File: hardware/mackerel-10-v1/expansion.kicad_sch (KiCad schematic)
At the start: 0 parts

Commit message: Rough layout of components on PCB
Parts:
- added C11, C12: 1000uF, Capacitor_THT:CP_Radial_D8.0mm_P3.50mm, symbol Device:C_Polarized
- added J10, J11: Conn_02x20_Odd_Even, Connector_IDC:IDC-Header_2x20_P2.54mm_Vertical, symbol Connector_Generic:Conn_02x20_Odd_Even
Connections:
- new net +5V: C11.1, C12.1, J10.1 (Pin_1), J10.2 (Pin_2), J11.1 (Pin_1), J11.2 (Pin_2)
- new net A1: J10.13 (Pin_13)
- new net A10: J10.28 (Pin_28)
- new net A11: J10.29 (Pin_29)
- new net A12: J10.30 (Pin_30)
- new net A13: J10.31 (Pin_31)
- new net A14: J10.32 (Pin_32)
- new net A15: J10.33 (Pin_33)
- new net A16: J10.34 (Pin_34)
- new net A17: J10.35 (Pin_35)
- new net A18: J10.36 (Pin_36)
- new net A19: J10.37 (Pin_37)
- new net A2: J10.14 (Pin_14)
- new net A20: J10.26 (Pin_26)
- new net A21: J10.25 (Pin_25)
- new net A22: J10.24 (Pin_24)
- new net A23: J10.23 (Pin_23)
- new net A3: J10.15 (Pin_15)
- new net A4: J10.16 (Pin_16)
- new net A5: J10.17 (Pin_17)
- new net A6: J10.18 (Pin_18)
- new net A7: J10.19 (Pin_19)
- new net A8: J10.20 (Pin_20)
- new net A9: J10.27 (Pin_27)
- new net CLK_CPU: J11.35 (Pin_35)
- new net D0: J11.5 (Pin_5)
- new net D1: J11.6 (Pin_6)
- new net D10: J10.7 (Pin_7)
- new net D11: J10.8 (Pin_8)
- new net D12: J10.9 (Pin_9)
- new net D13: J10.10 (Pin_10)
- new net D14: J10.11 (Pin_11)
- new net D15: J10.12 (Pin_12)
- new net D2: J11.7 (Pin_7)
- new net D3: J11.8 (Pin_8)
- new net D4: J11.9 (Pin_9)
- new net D5: J11.10 (Pin_10)
- new net D6: J11.11 (Pin_11)
- new net D7: J11.12 (Pin_12)
- new net D8: J10.5 (Pin_5)
- new net D9: J10.6 (Pin_6)
- new net GND: C11.2, C12.2, J10.21 (Pin_21), J10.22 (Pin_22), J10.3 (Pin_3), J10.38 (Pin_38), J10.39 (Pin_39), J10.4 (Pin_4), J10.40 (Pin_40), J11.23 (Pin_23), J11.24 (Pin_24), J11.3 (Pin_3), J11.33 (Pin_33), J11.34 (Pin_34), J11.39 (Pin_39), J11.4 (Pin_4), J11.40 (Pin_40)
- new net R/W: J11.14 (Pin_14)
- new net /AS: J11.13 (Pin_13)
- new net /BERR: J11.17 (Pin_17)
- new net /DTACK_EXP: J11.21 (Pin_21)
- new net /EXP: J11.19 (Pin_19)
- new net /IACK_EXP: J11.22 (Pin_22)
- new net /IRQ_EXP: J11.20 (Pin_20)
- new net /LDS: J11.16 (Pin_16)
- new net /RESET: J11.37 (Pin_37), J11.38 (Pin_38)
- new net /UDS: J11.15 (Pin_15)
- new net /VPA: J11.18 (Pin_18)

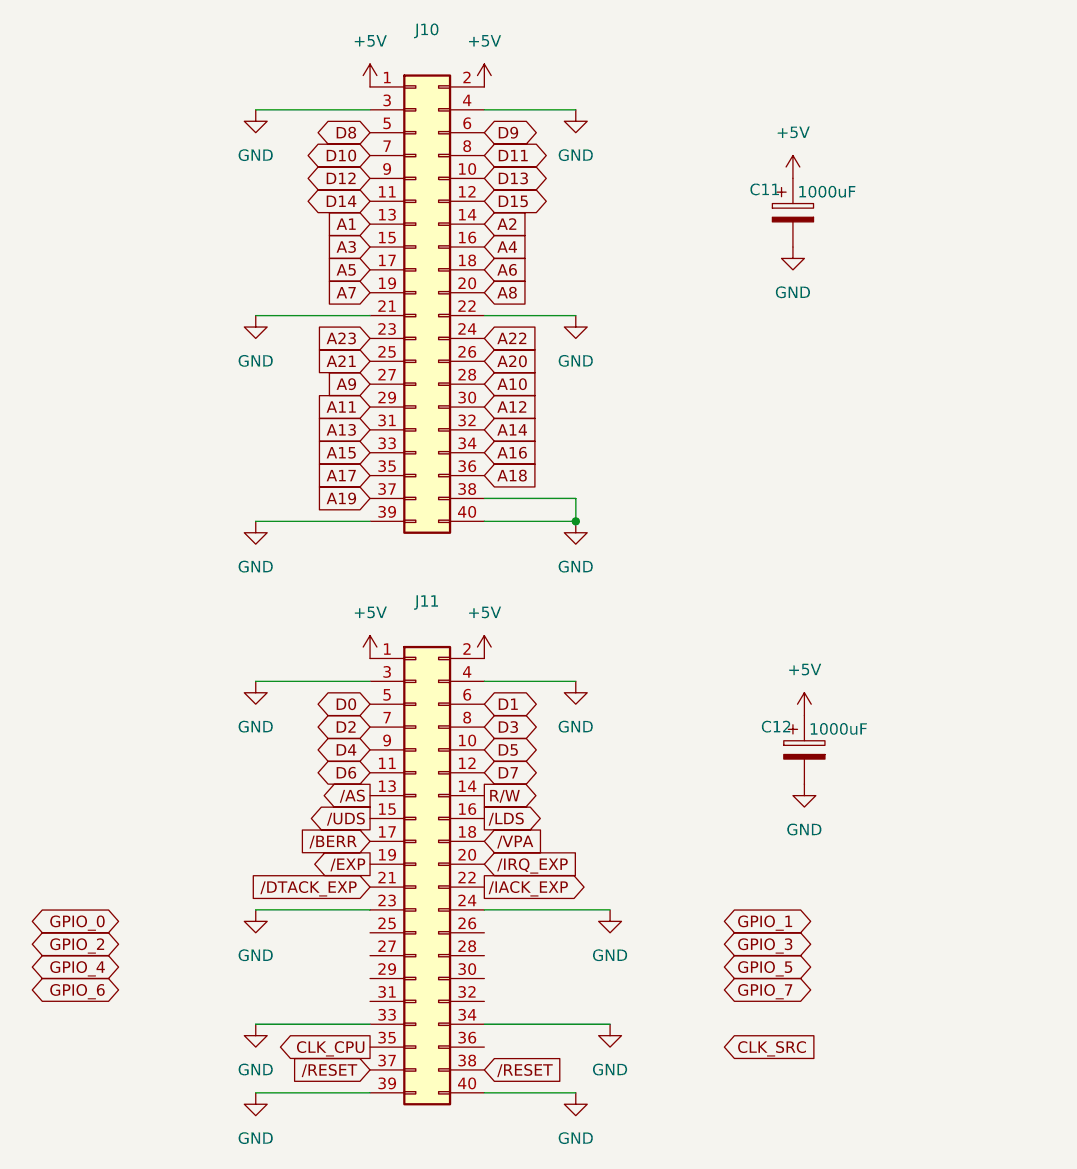
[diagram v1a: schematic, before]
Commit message: Settled on mini ITX form factor
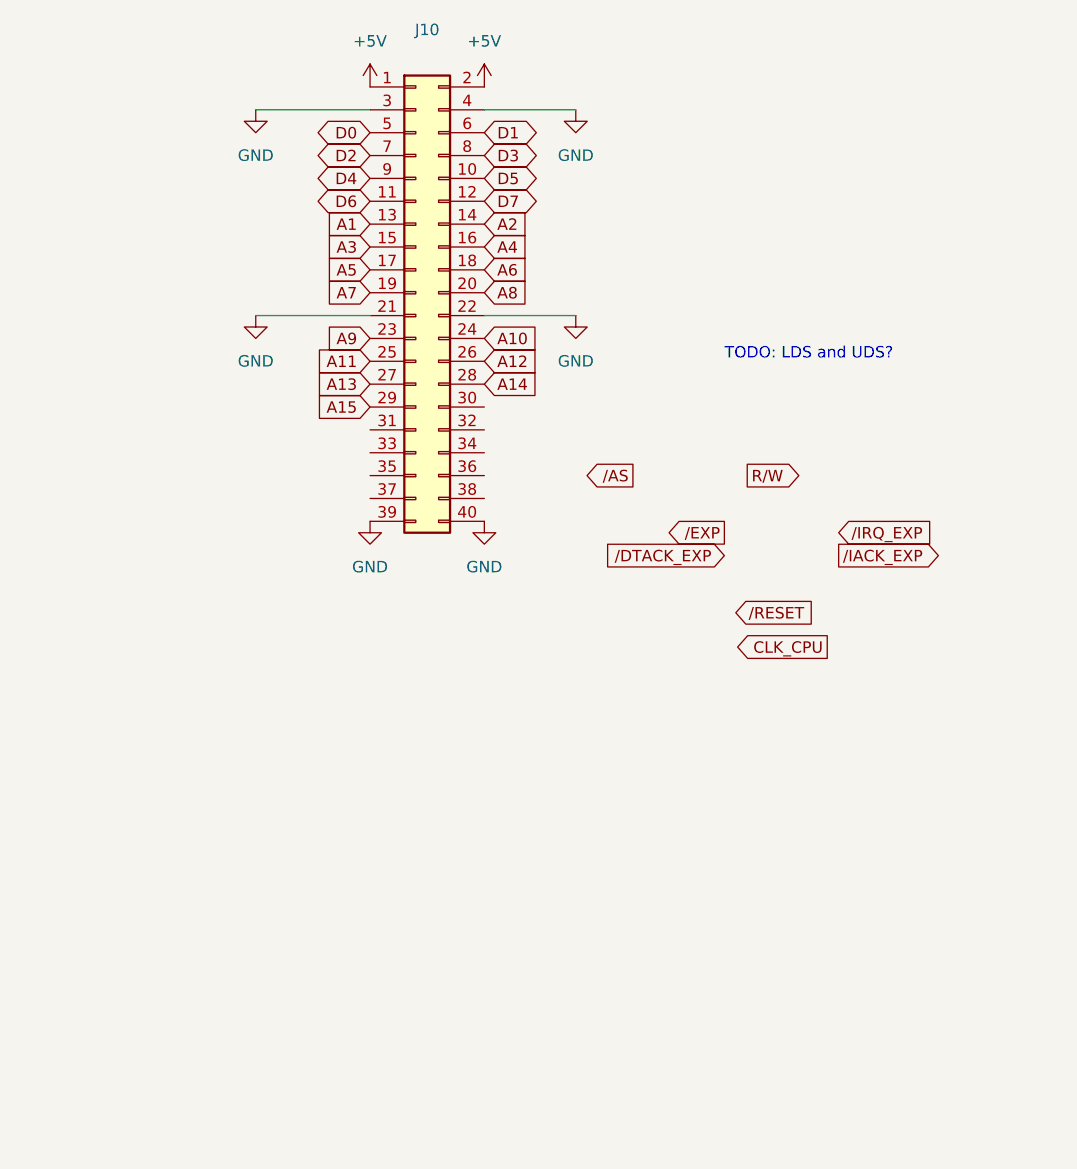
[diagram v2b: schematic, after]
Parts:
- removed C11, C12: 1000uF, Capacitor_THT:CP_Radial_D8.0mm_P3.50mm, symbol Device:C_Polarized
- removed J11: Conn_02x20_Odd_Even, Connector_IDC:IDC-Header_2x20_P2.54mm_Vertical, symbol Connector_Generic:Conn_02x20_Odd_Even
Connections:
- net A20 is gone; now on net A12: J10.26 (Pin_26)
- net A21 is gone; now on net A11: J10.25 (Pin_25)
- net A22 is gone; now on net A10: J10.24 (Pin_24)
- net A23 is gone; now on net A9: J10.23 (Pin_23)
- net D10 is gone; now on net D2: J10.7 (Pin_7)
- net D11 is gone; now on net D3: J10.8 (Pin_8)
- net D12 is gone; now on net D4: J10.9 (Pin_9)
- net D13 is gone; now on net D5: J10.10 (Pin_10)
- net D14 is gone; now on net D6: J10.11 (Pin_11)
- net D15 is gone; now on net D7: J10.12 (Pin_12)
- net D8 is gone; now on net D0: J10.5 (Pin_5)
- net D9 is gone; now on net D1: J10.6 (Pin_6)
- net A10: no longer J10.28 (Pin_28)
- net A11: no longer J10.29 (Pin_29)
- net A12: no longer J10.30 (Pin_30)
- net A13: now also J10.27 (Pin_27); no longer J10.31 (Pin_31)
- net A14: now also J10.28 (Pin_28); no longer J10.32 (Pin_32)
- net A15: now also J10.29 (Pin_29); no longer J10.33 (Pin_33)
- net A9: no longer J10.27 (Pin_27)
- net GND: no longer J10.38 (Pin_38)
- net A16: no longer names the net of J10.34 (Pin_34)
- net A17: no longer names the net of J10.35 (Pin_35)
- net A18: no longer names the net of J10.36 (Pin_36)
- net A19: no longer names the net of J10.37 (Pin_37)
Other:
- note added: "TODO: LDS and UDS?"

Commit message: Another layout plan
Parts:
- removed J10: Conn_02x20_Odd_Even, Connector_IDC:IDC-Header_2x20_P2.54mm_Vertical, symbol Connector_Generic:Conn_02x20_Odd_Even
- added J17: Conn_02x30_Counter_Clockwise, Connector_IDC:IDC-Header_2x30_P2.54mm_Vertical, symbol Connector_Generic:Conn_02x30_Counter_Clockwise
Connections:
- net +5V: now also J17.1 (Pin_1), J17.60 (Pin_60)
- net A1: now also J17.7 (Pin_7)
- net A10: now also J17.49 (Pin_49)
- net A11: now also J17.13 (Pin_13)
- net A12: now also J17.48 (Pin_48)
- net A13: now also J17.14 (Pin_14)
- net A14: now also J17.47 (Pin_47)
- net A15: now also J17.15 (Pin_15)
- net A2: now also J17.54 (Pin_54)
- net A3: now also J17.8 (Pin_8)
- net A4: now also J17.53 (Pin_53)
- net A5: now also J17.9 (Pin_9)
- net A6: now also J17.52 (Pin_52)
- net A7: now also J17.10 (Pin_10)
- net A8: now also J17.51 (Pin_51)
- net A9: now also J17.12 (Pin_12)
- net D0: now also J17.3 (Pin_3)
- net D1: now also J17.58 (Pin_58)
- net D2: now also J17.4 (Pin_4)
- net D3: now also J17.57 (Pin_57)
- net D4: now also J17.5 (Pin_5)
- net D5: now also J17.56 (Pin_56)
- net D6: now also J17.6 (Pin_6)
- net D7: now also J17.55 (Pin_55)
- net GND: now also J17.11 (Pin_11), J17.2 (Pin_2), J17.20 (Pin_20), J17.41 (Pin_41), J17.50 (Pin_50), J17.59 (Pin_59)
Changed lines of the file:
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@@
-	)
-	(symbol
-		(lib_id "Connector_Generic:Conn_02x20_Odd_Even")
-		(at 76.2 73.66 0)
-		(unit 1)
-		(exclude_from_sim no)
-		(in_bom yes)
-		(on_board yes)
-		(dnp no)
-		(fields_autoplaced yes)
-		(property "Reference" "J10"
-			(at 77.47 44.45 0)
-			(effects
-				(font
-					(size 1.27 1.27)
-				)
-			)
-		)
-		(property "Value" "Conn_02x20_Odd_Even"
-			(at 77.47 46.99 0)
-			(effects
-				(font
-					(size 1.27 1.27)
-				)
-				(hide yes)
-			)
-		)
-		(property "Footprint" "Connector_IDC:IDC-Header_2x20_P2.54mm_Vertical"
-			(at 76.2 73.66 0)
-			(effects
-				(font
-					(size 1.27 1.27)
-				)
-				(hide yes)
-			)
-		)
-		(property "Datasheet" "~"
-			(at 76.2 73.66 0)
-			(effects
-				(font
-					(size 1.27 1.27)
-				)
-				(hide yes)
-			)
-		)
-		(property "Description" "Generic connector, double row, 02x20, odd/even pin numbering scheme (row 1 odd numbers, row 2 even numbers), script generated (kicad-library-utils/schlib/autogen/connector/)"
-			(at 76.2 73.66 0)
-			(effects
-				(font
-					(size 1.27 1.27)
-				)
-				(hide yes)
-			)
-		)
-		(pin "27"
-		)
-		(pin "39"
-		)
-		(pin "18"
-		)
-		(pin "26"
-		)
-		(pin "29"
-		)
-		(pin "9"
-		)
-		(pin "40"
-		)
-		(pin "20"
-		)
-		(pin "19"
-		)
-		(pin "21"
-		)
-		(pin "37"
-		)
-		(pin "24"
-		)
-		(pin "34"
-		)
-		(pin "33"
-		)
-		(pin "35"
-		)
-		(pin "14"
-		)
-		(pin "23"
-		)
-		(pin "32"
-		)
-		(pin "3"
-		)
-		(pin "22"
-		)
-		(pin "17"
-		)
-		(pin "25"
-		)
-		(pin "30"
-		)
-		(pin "7"
-		)
-		(pin "38"
-		)
-		(pin "8"
-		)
-		(pin "4"
-		)
-		(pin "6"
-		)
-		(pin "5"
-		)
-		(pin "36"
-		)
-		(pin "12"
-		)
-		(pin "13"
-		)
-		(pin "10"
-		)
-		(pin "11"
-		)
-		(pin "1"
-		)
-		(pin "2"
-		)
-		(pin "31"
-		)
-		(pin "16"
-		)
-		(pin "15"
-		)
-		(pin "28"
-		)
-		(instances
-			(project "mackerel-10-v1"
-				(path "/0a8f74be-008b-4256-a2d9-73a458311ea0/eb382f11-e263-426f-affb-26cce29b45e2"
-					(reference "J10")
-					(unit 1)
-				)
-			)
-		)
 	)
 	(symbol
@@
 					(unit 1)
 				)
+			)
+		)
+	)
+	(symbol
+		(lib_id "Connector_Generic:Conn_02x30_Counter_Clockwise")
+		(at 76.2 86.36 0)
+		(unit 1)
+		(exclude_from_sim no)
+		(in_bom yes)
+		(on_board yes)
+		(dnp no)
+		(fields_autoplaced yes)
+		(property "Reference" "J17"
+			(at 77.47 44.45 0)
+			(effects
+				(font
+					(size 1.27 1.27)
+				)
+			)
+		)
+		(property "Value" "Conn_02x30_Counter_Clockwise"
+			(at 77.47 46.99 0)
+			(effects
+				(font
+					(size 1.27 1.27)
+				)
+			)
+		)
+		(property "Footprint" "Connector_IDC:IDC-Header_2x30_P2.54mm_Vertical"
+			(at 76.2 86.36 0)
+			(effects
+				(font
+					(size 1.27 1.27)
+				)
+				(hide yes)
+			)
+		)
+		(property "Datasheet" "~"
+			(at 76.2 86.36 0)
+			(effects
+				(font
+					(size 1.27 1.27)
+				)
+				(hide yes)
+			)
+		)
+		(property "Description" "Generic connector, double row, 02x30, counter clockwise pin numbering scheme (similar to DIP package numbering), script generated (kicad-library-utils/schlib/autogen/connector/)"
+			(at 76.2 86.36 0)
+			(effects
+				(font
+					(size 1.27 1.27)
+				)
+				(hide yes)
+			)
+		)
+		(pin "5"
+		)
+		(pin "33"
+		)
+		(pin "29"
+		)
+		(pin "2"
+		)
+		(pin "32"
+		)
+		(pin "44"
+		)
+		(pin "50"
+		)
+		(pin "17"
+		)
+		(pin "57"
+		)
+		(pin "56"
+		)
+		(pin "19"
+		)
+		(pin "7"
+		)
+		(pin "6"
+		)
+		(pin "31"
+		)
+		(pin "48"
+		)
+		(pin "12"
+		)
+		(pin "60"
+		)
+		(pin "8"
+		)
+		(pin "13"
+		)
+		(pin "14"
+		)
+		(pin "45"
+		)
+		(pin "4"
+		)
+		(pin "46"
+		)
+		(pin "1"
+		)
+		(pin "16"
+		)
+		(pin "37"
+		)
+		(pin "52"
+		)
+		(pin "34"
+		)
+		(pin "59"
+		)
+		(pin "58"
+		)
+		(pin "42"
+		)
+		(pin "35"
+		)
+		(pin "20"
+		)
+		(pin "51"
+		)
+		(pin "54"
+		)
+		(pin "47"
+		)
+		(pin "28"
+		)
+		(pin "53"
+		)
+		(pin "22"
+		)
+		(pin "39"
+		)
+		(pin "40"
+		)
+		(pin "38"
+		)
+		(pin "26"
+		)
+		(pin "41"
+		)
+		(pin "11"
+		)
+		(pin "25"
+		)
+		(pin "23"
+		)
+		(pin "9"
+		)
+		(pin "30"
+		)
+		(pin "24"
+		)
+		(pin "15"
+		)
+		(pin "55"
+		)
+		(pin "36"
+		)
+		(pin "43"
+		)
+		(pin "27"
+		)
+		(pin "21"
+		)
+		(pin "18"
+		)
+		(pin "49"
+		)
+		(pin "10"
+		)
+		(pin "3"
+		)
+		(instances
+			(project ""
+				(path "/0a8f74be-008b-4256-a2d9-73a458311ea0/eb382f11-e263-426f-affb-26cce29b45e2"
+					(reference "J17")
+					(unit 1)
+				)

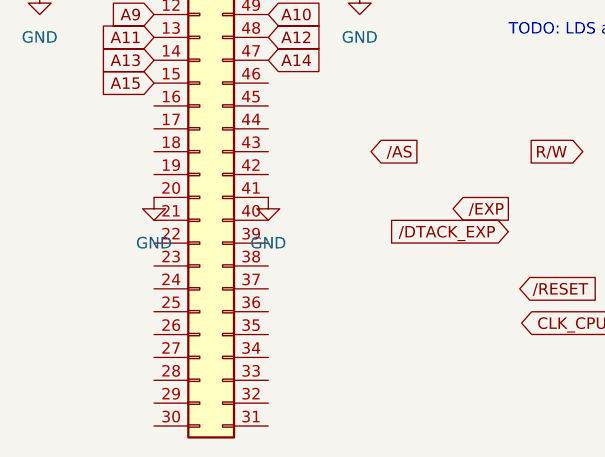
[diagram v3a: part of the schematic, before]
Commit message: half routed
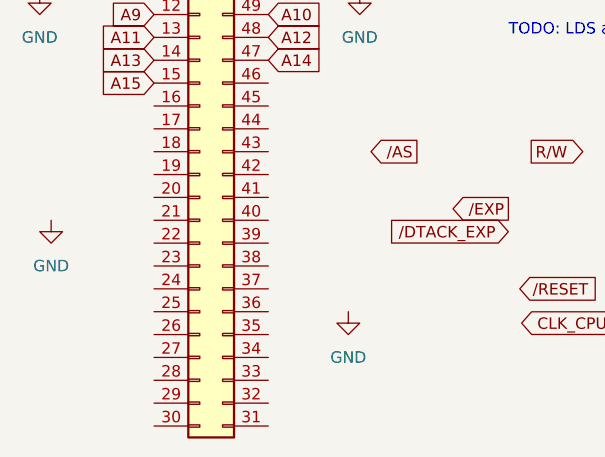
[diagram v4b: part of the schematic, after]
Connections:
- net GND: no longer J17.20 (Pin_20), J17.41 (Pin_41)
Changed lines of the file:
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@@
 	(symbol
 		(lib_id "power:GND")
-		(at 83.82 99.06 0)
+		(at 92.71 111.76 0)
 		(unit 1)
 		(exclude_from_sim no)
@@
 		(fields_autoplaced yes)
 		(property "Reference" "#PWR091"
-			(at 83.82 105.41 0)
+			(at 92.71 118.11 0)
 			(effects
 				(font
@@
 		)
 		(property "Value" "GND"
-			(at 83.82 104.14 0)
+			(at 92.71 116.84 0)
 			(effects
 				(font
@@
 		)
 		(property "Footprint" ""
-			(at 83.82 99.06 0)
+			(at 92.71 111.76 0)
 			(effects
 				(font
@@
 		)
 		(property "Datasheet" ""
-			(at 83.82 99.06 0)
+			(at 92.71 111.76 0)
 			(effects
 				(font
@@
 		)
 		(property "Description" "Power symbol creates a global label with name \"GND\" , ground"
-			(at 83.82 99.06 0)
+			(at 92.71 111.76 0)
 			(effects
 				(font
@@
 	(symbol
 		(lib_id "power:GND")
-		(at 71.12 99.06 0)
+		(at 59.69 101.6 0)
 		(unit 1)
 		(exclude_from_sim no)
@@
 		(fields_autoplaced yes)
 		(property "Reference" "#PWR080"
-			(at 71.12 105.41 0)
+			(at 59.69 107.95 0)
 			(effects
 				(font
@@
 		)
 		(property "Value" "GND"
-			(at 71.12 104.14 0)
+			(at 59.69 106.68 0)
 			(effects
 				(font
@@
 		)
 		(property "Footprint" ""
-			(at 71.12 99.06 0)
+			(at 59.69 101.6 0)
 			(effects
 				(font
@@
 		)
 		(property "Datasheet" ""
-			(at 71.12 99.06 0)
+			(at 59.69 101.6 0)
 			(effects
 				(font
@@
 		)
 		(property "Description" "Power symbol creates a global label with name \"GND\" , ground"
-			(at 71.12 99.06 0)
+			(at 59.69 101.6 0)
 			(effects
 				(font

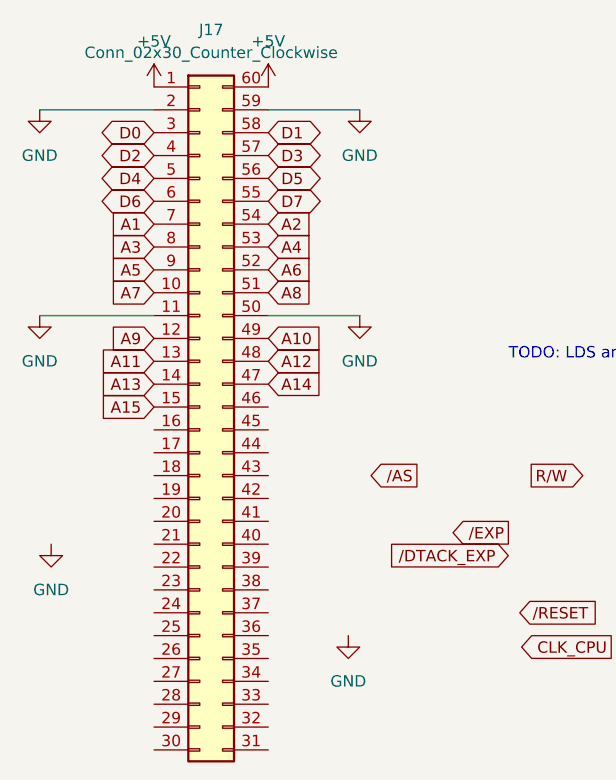
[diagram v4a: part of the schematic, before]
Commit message: Glue logic CPLD almost fully routed
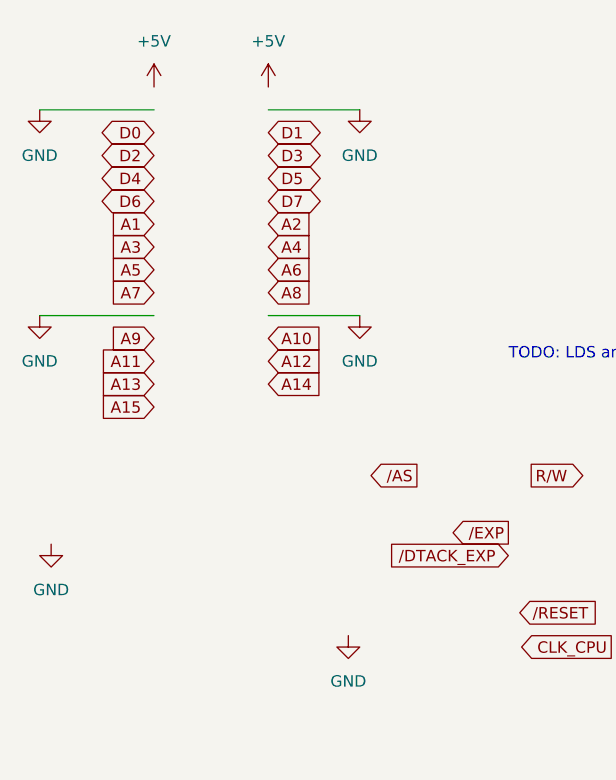
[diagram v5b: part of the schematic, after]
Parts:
- removed J17: Conn_02x30_Counter_Clockwise, Connector_IDC:IDC-Header_2x30_P2.54mm_Vertical, symbol Connector_Generic:Conn_02x30_Counter_Clockwise
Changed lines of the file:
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@@
-		)
-	)
-	(symbol
-		(lib_id "Connector_Generic:Conn_02x30_Counter_Clockwise")
-		(at 76.2 86.36 0)
-		(unit 1)
-		(exclude_from_sim no)
-		(in_bom yes)
-		(on_board yes)
-		(dnp no)
-		(fields_autoplaced yes)
-		(property "Reference" "J17"
-			(at 77.47 44.45 0)
-			(effects
-				(font
-					(size 1.27 1.27)
-				)
-			)
-		)
-		(property "Value" "Conn_02x30_Counter_Clockwise"
-			(at 77.47 46.99 0)
-			(effects
-				(font
-					(size 1.27 1.27)
-				)
-			)
-		)
-		(property "Footprint" "Connector_IDC:IDC-Header_2x30_P2.54mm_Vertical"
-			(at 76.2 86.36 0)
-			(effects
-				(font
-					(size 1.27 1.27)
-				)
-				(hide yes)
-			)
-		)
-		(property "Datasheet" "~"
-			(at 76.2 86.36 0)
-			(effects
-				(font
-					(size 1.27 1.27)
-				)
-				(hide yes)
-			)
-		)
-		(property "Description" "Generic connector, double row, 02x30, counter clockwise pin numbering scheme (similar to DIP package numbering), script generated (kicad-library-utils/schlib/autogen/connector/)"
-			(at 76.2 86.36 0)
-			(effects
-				(font
-					(size 1.27 1.27)
-				)
-				(hide yes)
-			)
-		)
-		(pin "5"
-		)
-		(pin "33"
-		)
-		(pin "29"
-		)
-		(pin "2"
-		)
-		(pin "32"
-		)
-		(pin "44"
-		)
-		(pin "50"
-		)
-		(pin "17"
-		)
-		(pin "57"
-		)
-		(pin "56"
-		)
-		(pin "19"
-		)
-		(pin "7"
-		)
-		(pin "6"
-		)
-		(pin "31"
-		)
-		(pin "48"
-		)
-		(pin "12"
-		)
-		(pin "60"
-		)
-		(pin "8"
-		)
-		(pin "13"
-		)
-		(pin "14"
-		)
-		(pin "45"
-		)
-		(pin "4"
-		)
-		(pin "46"
-		)
-		(pin "1"
-		)
-		(pin "16"
-		)
-		(pin "37"
-		)
-		(pin "52"
-		)
-		(pin "34"
-		)
-		(pin "59"
-		)
-		(pin "58"
-		)
-		(pin "42"
-		)
-		(pin "35"
-		)
-		(pin "20"
-		)
-		(pin "51"
-		)
-		(pin "54"
-		)
-		(pin "47"
-		)
-		(pin "28"
-		)
-		(pin "53"
-		)
-		(pin "22"
-		)
-		(pin "39"
-		)
-		(pin "40"
-		)
-		(pin "38"
-		)
-		(pin "26"
-		)
-		(pin "41"
-		)
-		(pin "11"
-		)
-		(pin "25"
-		)
-		(pin "23"
-		)
-		(pin "9"
-		)
-		(pin "30"
-		)
-		(pin "24"
-		)
-		(pin "15"
-		)
-		(pin "55"
-		)
-		(pin "36"
-		)
-		(pin "43"
-		)
-		(pin "27"
-		)
-		(pin "21"
-		)
-		(pin "18"
-		)
-		(pin "49"
-		)
-		(pin "10"
-		)
-		(pin "3"
-		)
-		(instances
-			(project ""
-				(path "/0a8f74be-008b-4256-a2d9-73a458311ea0/eb382f11-e263-426f-affb-26cce29b45e2"
-					(reference "J17")
-					(unit 1)
-				)
-			)
 		)
 	)
